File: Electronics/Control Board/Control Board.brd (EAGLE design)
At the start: 160 x 100 mm, 0 parts

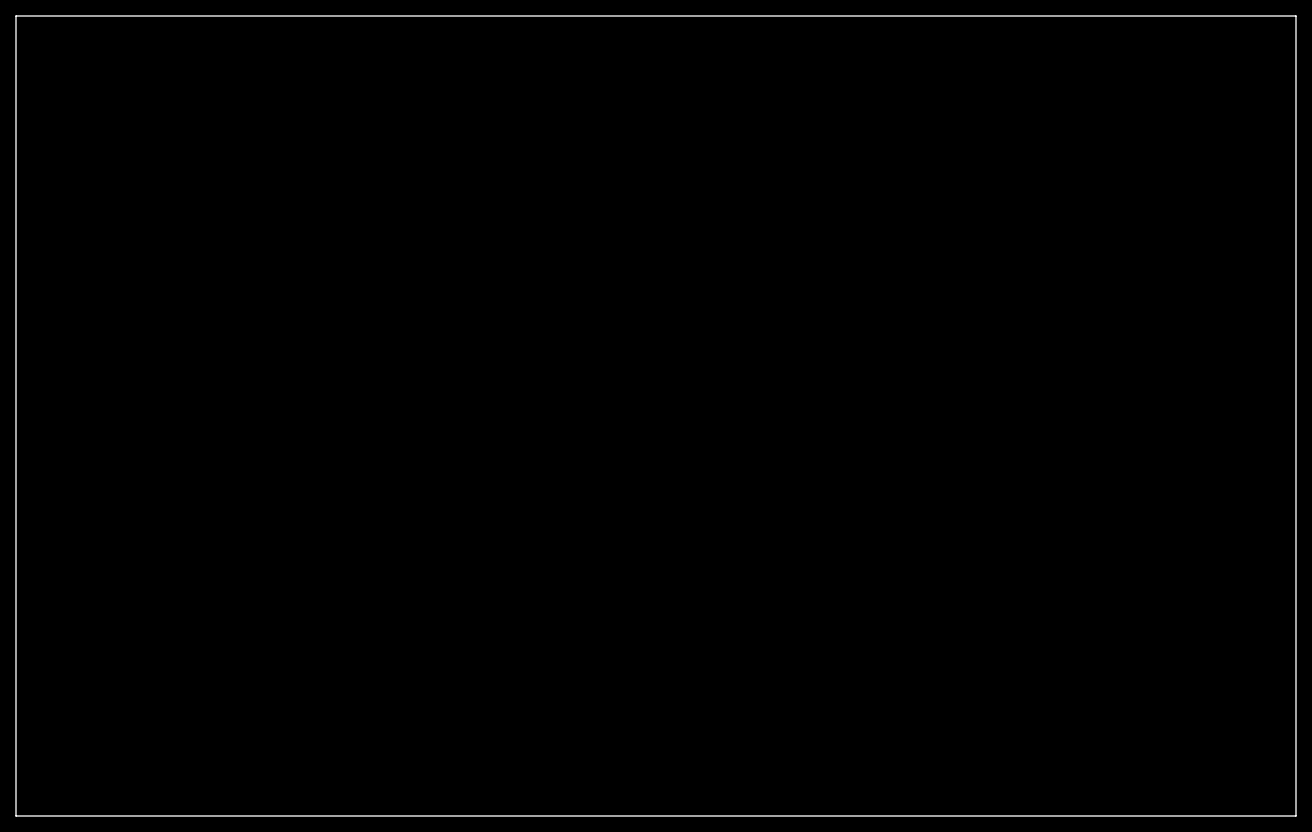
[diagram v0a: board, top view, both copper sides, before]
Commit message: Added filler for control module and flushed out body sketch some more. Added two more displays
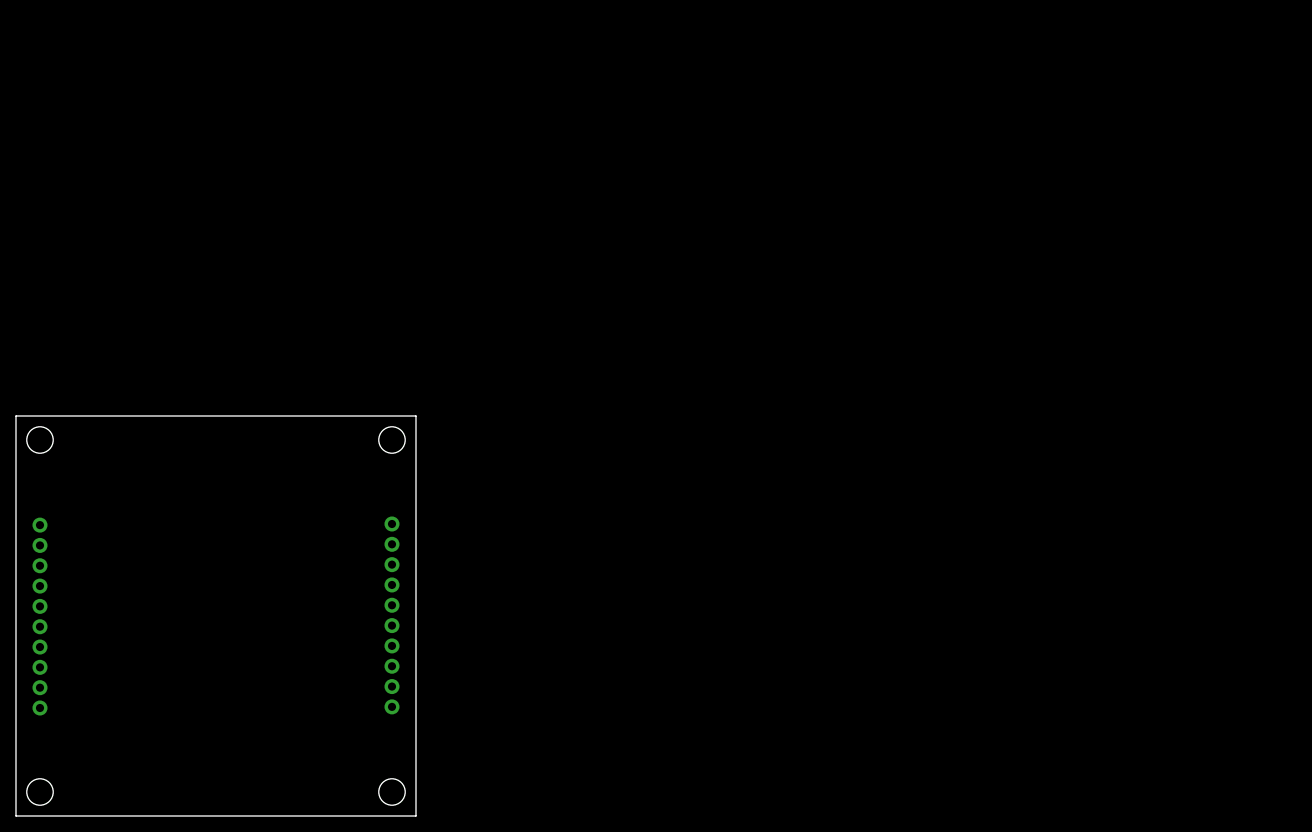
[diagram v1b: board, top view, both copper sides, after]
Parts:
- added JP1, JP2: M10-M20-9991046, Control Board Library:M20-9991046
- added STANDOFF1, STANDOFF2, STANDOFF3, STANDOFF4: STAND-OFF, Resistor Module Library:STAND-OFF
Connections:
- new net 5V: JP1.6
- new net 5V_2: JP2.6
- new net EEPROM_CS_L: JP1.1
- new net EEPROM_MISO: JP1.4
- new net EEPROM_MOSI: JP1.2
- new net EEPROM_SCK: JP1.3
- new net GND: JP1.5
- new net GND_2: JP2.5
- new net R_IN: JP2.1
- new net R_OUT: JP2.2
- new net SERIAL_CLK: JP1.8
- new net SERIAL_CLK_2: JP2.8
- new net SERIAL_IN: JP2.4
- new net SERIAL_LATCH: JP1.9
- new net SERIAL_LATCH_2: JP2.9
- new net SERIAL_MR_L: JP1.7
- new net SERIAL_MR_L_2: JP2.7
- new net SERIAL_OE_L: JP1.10
- new net SERIAL_OE_L_2: JP2.10
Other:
- board size 160 x 100 mm -> 50 x 50 mm

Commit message: Started work on control board.
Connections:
- net SERIAL_IN renamed SERIAL_OUT
- removed net 5V_2: JP2.6
- removed net GND_2: JP2.5
- removed net SERIAL_CLK_2: JP2.8
- removed net SERIAL_LATCH_2: JP2.9
- removed net SERIAL_MR_L_2: JP2.7
- removed net SERIAL_OE_L_2: JP2.10
- net 5V: now also JP2.6
- net GND: now also JP2.5
- net R_IN: now also JP2.2; no longer JP2.1
- net R_OUT: now also JP2.1; no longer JP2.2
- net SERIAL_CLK: now also JP2.8
- net SERIAL_LATCH: now also JP2.9
- net SERIAL_MR_L: now also JP2.7
- net SERIAL_OE_L: now also JP2.10
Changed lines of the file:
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@@
 </variantdefs>
 <classes>
-<class number="0" name="default" width="0" drill="0">
+<class number="0" name="default" width="0.2032" drill="0.4064">
+<clearance class="0" value="0.2032"/>
+</class>
+<class number="1" name="power" width="0.6096" drill="0.4064">
+<clearance class="1" value="0.2032"/>
+</class>
+<class number="2" name="gnd" width="0.3048" drill="0.4064">
+<clearance class="2" value="0.2032"/>
+</class>
+<class number="3" name="power usb" width="0.508" drill="0.4064">
+<clearance class="3" value="0.2032"/>
 </class>
 </classes>
@@
 <signal name="SERIAL_LATCH">
 <contactref element="JP1" pad="9"/>
+<contactref element="JP2" pad="9"/>
+<wire x1="3" y1="33.82" x2="47" y2="16.18" width="0" layer="19" extent="1-1"/>
 </signal>
 <signal name="SERIAL_OE_L">
 <contactref element="JP1" pad="10"/>
+<contactref element="JP2" pad="10"/>
+<wire x1="3" y1="36.36" x2="47" y2="13.64" width="0" layer="19" extent="1-1"/>
 </signal>
 <signal name="EEPROM_MOSI">
@@
 <signal name="5V">
 <contactref element="JP1" pad="6"/>
+<contactref element="JP2" pad="6"/>
+<wire x1="3" y1="26.2" x2="47" y2="23.8" width="0" layer="19" extent="1-1"/>
 </signal>
 <signal name="GND">
 <contactref element="JP1" pad="5"/>
-</signal>
-<signal name="SERIAL_IN">
+<contactref element="JP2" pad="5"/>
+<wire x1="3" y1="23.66" x2="47" y2="26.34" width="0" layer="19" extent="1-1"/>
+</signal>
+<signal name="SERIAL_OUT">
 <contactref element="JP2" pad="4"/>
-</signal>
-<signal name="SERIAL_OE_L_2">
-<contactref element="JP2" pad="10"/>
-</signal>
-<signal name="SERIAL_LATCH_2">
-<contactref element="JP2" pad="9"/>
-</signal>
-<signal name="5V_2">
-<contactref element="JP2" pad="6"/>
-</signal>
-<signal name="GND_2">
-<contactref element="JP2" pad="5"/>
 </signal>
 <signal name="EEPROM_CS_L">
@@
 </signal>
 <signal name="R_IN">
-<contactref element="JP2" pad="1"/>
-</signal>
-<signal name="R_OUT">
 <contactref element="JP2" pad="2"/>
 </signal>
 <signal name="SERIAL_MR_L">
 <contactref element="JP1" pad="7"/>
-</signal>
-<signal name="SERIAL_MR_L_2">
 <contactref element="JP2" pad="7"/>
+<wire x1="3" y1="28.74" x2="47" y2="21.26" width="0" layer="19" extent="1-1"/>
 </signal>
 <signal name="SERIAL_CLK">
 <contactref element="JP1" pad="8"/>
-</signal>
-<signal name="SERIAL_CLK_2">
 <contactref element="JP2" pad="8"/>
+<wire x1="3" y1="31.28" x2="47" y2="18.72" width="0" layer="19" extent="1-1"/>
+</signal>
+<signal name="R_OUT">
+<contactref element="JP2" pad="1"/>
 </signal>
 </signals>

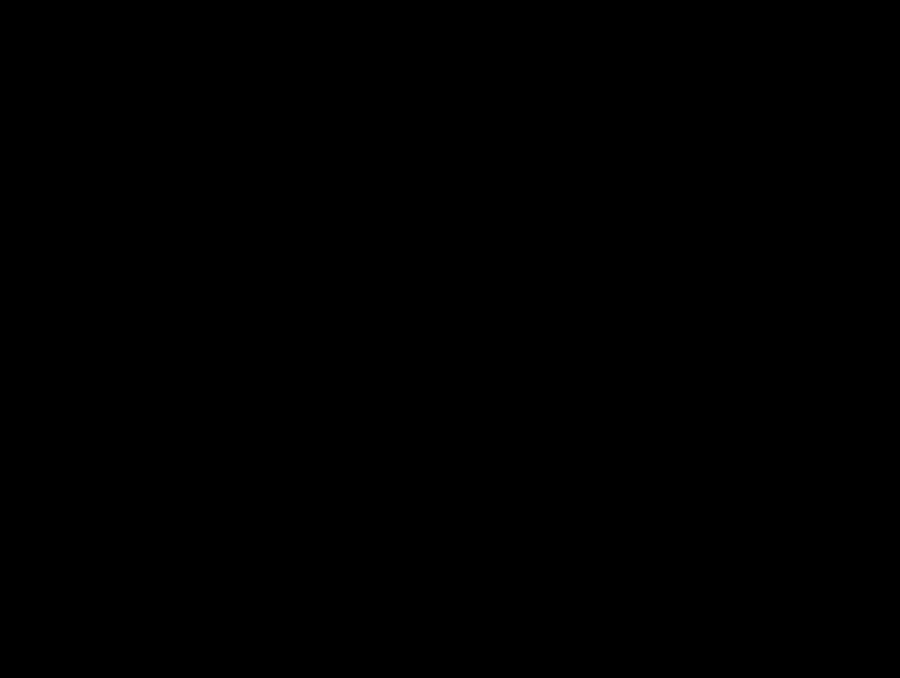
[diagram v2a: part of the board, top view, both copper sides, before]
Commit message: Selected 8U2 microchip for main controller. Don't need a lot of IO and needed included USB drive
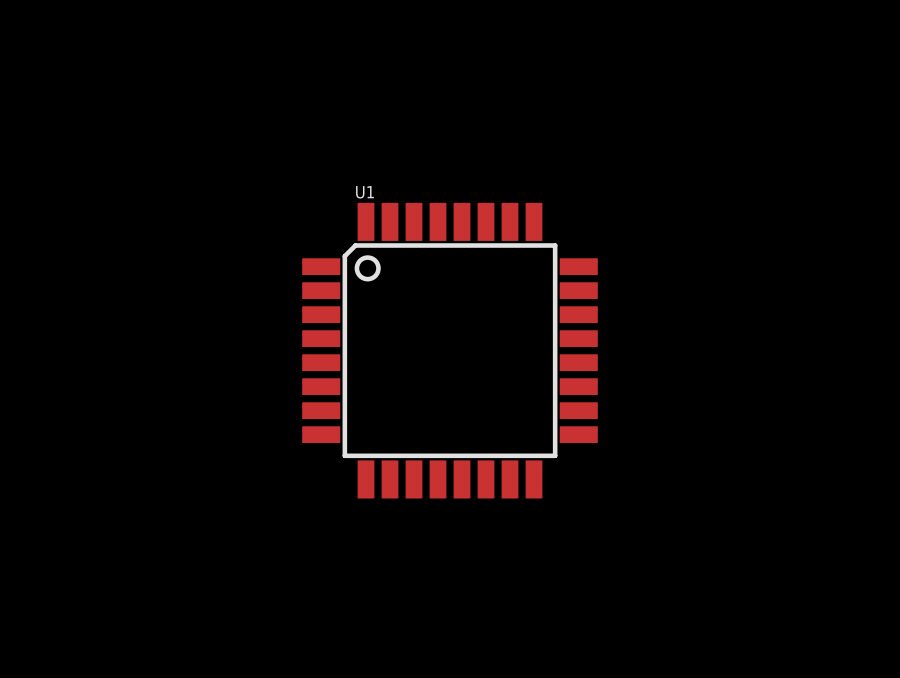
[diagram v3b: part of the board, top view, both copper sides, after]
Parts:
- added U1: ATMEGA8U2AU, Control Board Library:TQFP32-08
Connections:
- net 5V: now also U1.32, U1.4
- net GND: now also U1.28, U1.3
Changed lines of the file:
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@@
 <element name="JP1" library="Control Board Library" package="M20-9991046" value="M10-M20-9991046" x="3" y="13.5" rot="MR90"/>
 <element name="JP2" library="Control Board Library" package="M20-9991046" value="M10-M20-9991046" x="47" y="36.5" rot="MR270"/>
+<element name="U1" library="Control Board Library" package="TQFP32-08" value="ATMEGA8U2AU" x="25.4" y="25.4"/>
 </elements>
 <signals>
@@
 <contactref element="JP1" pad="6"/>
 <contactref element="JP2" pad="6"/>
+<contactref element="U1" pad="4"/>
+<contactref element="U1" pad="32"/>
 <wire x1="3" y1="26.2" x2="47" y2="23.8" width="0" layer="19" extent="1-1"/>
+<wire x1="22.6" y1="29.6926" x2="3" y2="26.2" width="0" layer="19" extent="1-1"/>
+<wire x1="21.1074" y1="25.8" x2="22.6" y2="29.6926" width="0" layer="19" extent="1-1"/>
 </signal>
 <signal name="GND">
 <contactref element="JP1" pad="5"/>
 <contactref element="JP2" pad="5"/>
+<contactref element="U1" pad="3"/>
+<contactref element="U1" pad="28"/>
 <wire x1="3" y1="23.66" x2="47" y2="26.34" width="0" layer="19" extent="1-1"/>
+<wire x1="25.8" y1="29.6926" x2="3" y2="23.66" width="0" layer="19" extent="1-1"/>
+<wire x1="21.1074" y1="26.6" x2="25.8" y2="29.6926" width="0" layer="19" extent="1-1"/>
 </signal>
 <signal name="SERIAL_OUT">
